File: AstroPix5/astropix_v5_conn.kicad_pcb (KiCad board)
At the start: 4 copper layers, 56.4 x 65.6 mm, 50 parts, among them J1 HBOut, J10 SPI_right, J12 Measures_Analog, J14 Bias, J2 Conn_01x05, J3 pcie_GECCO, J4 HBOut, J5 HBOut, J7 HV_in_external, J8 Conn_01x03, J9 SPI_left, U2 AstroPix5_split_powerring

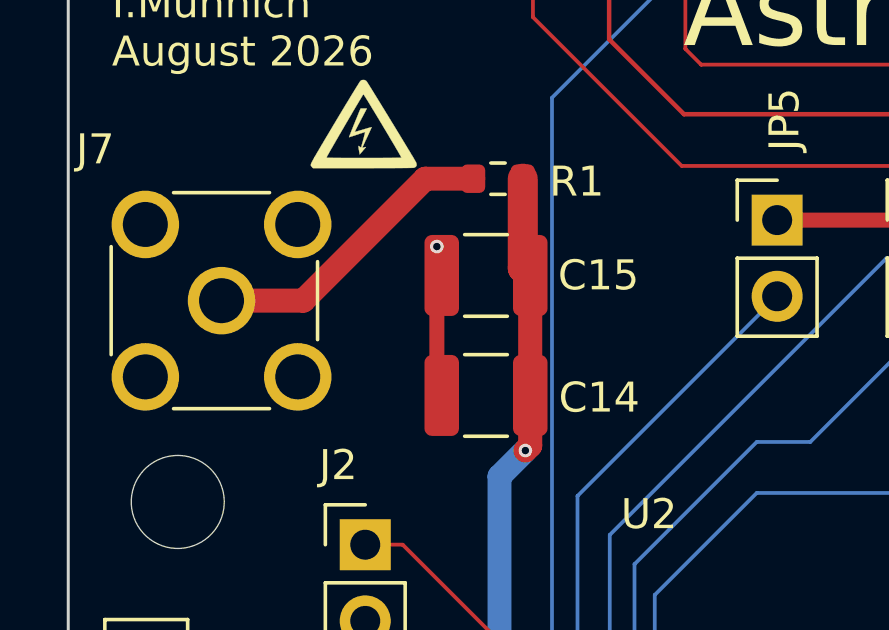
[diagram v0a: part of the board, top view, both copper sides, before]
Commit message: Move C15 via out of pad, regenerate fab outputs, add 3D renders (Macrofab drc)
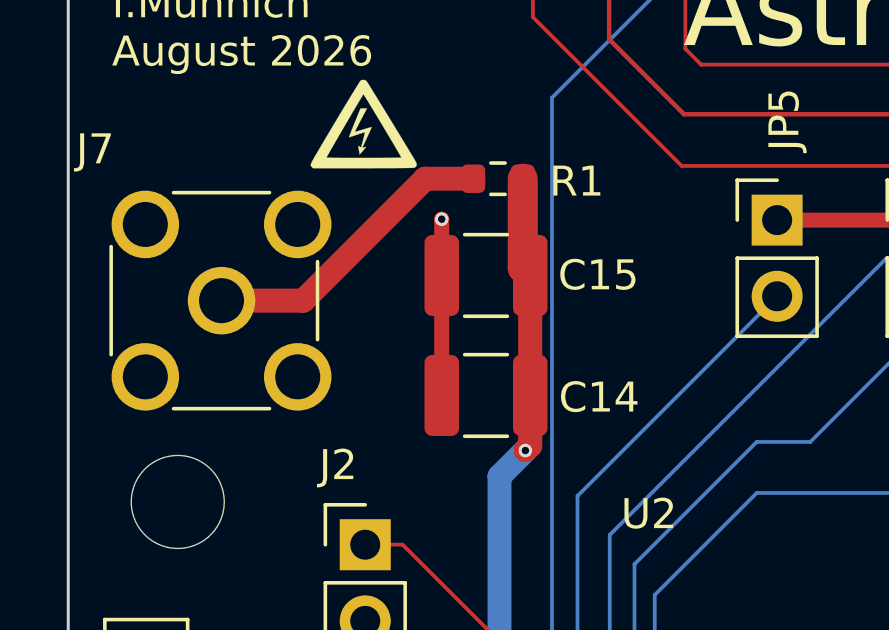
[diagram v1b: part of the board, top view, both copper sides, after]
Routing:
- net GND: track 89.8 -> 90.6 mm
